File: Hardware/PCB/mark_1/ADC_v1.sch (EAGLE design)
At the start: 13 parts, among them IC1 MCP3424, IC2 MCP23017SO, Q1 IRLML6402, Q2 IRLML6402, Q3 IRLML6402, Q4 IRLML6402

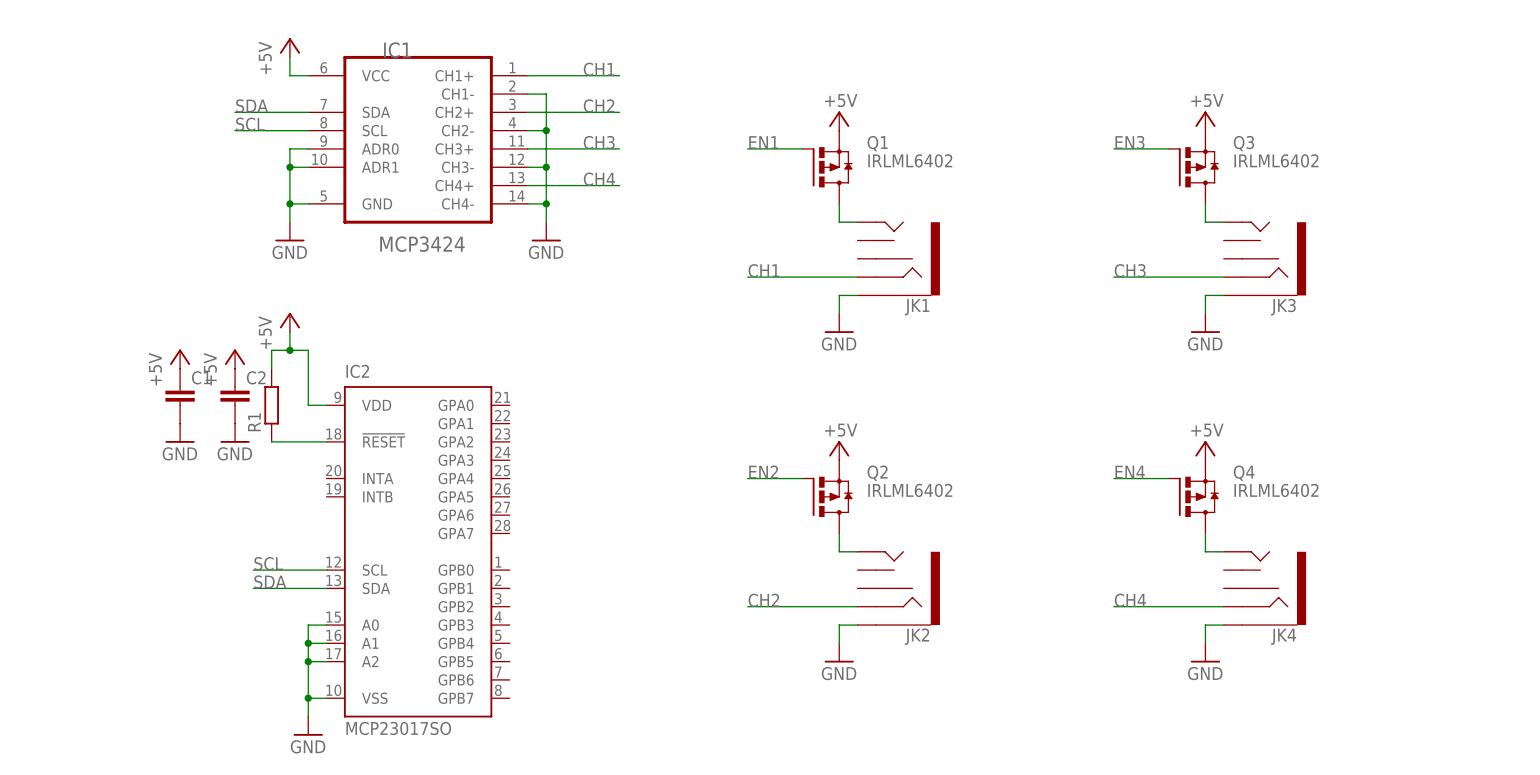
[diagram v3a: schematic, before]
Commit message: 
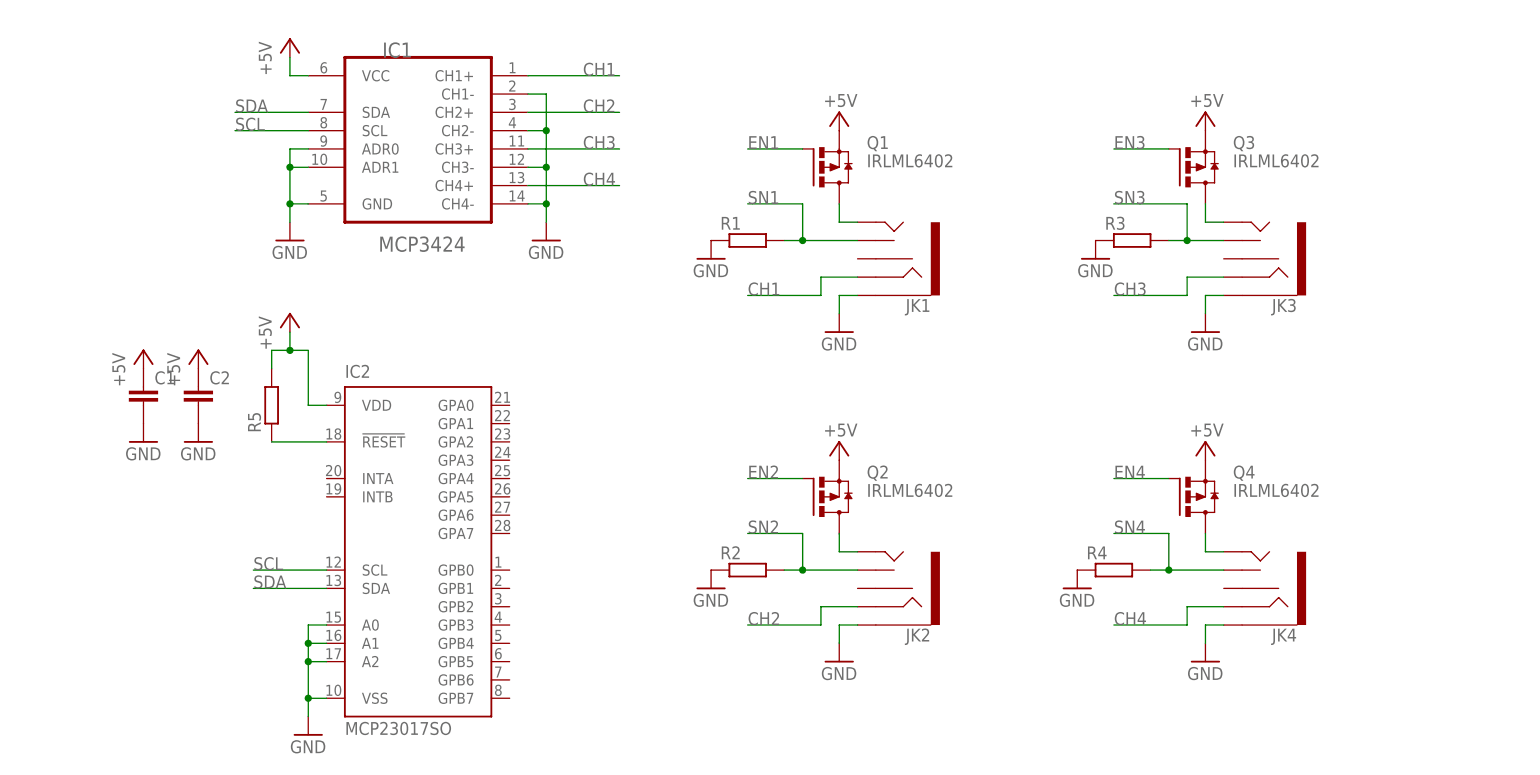
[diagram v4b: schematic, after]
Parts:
- added R2, R3, R4, R5: (no value), mark_1:R-EU_R0805
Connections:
- new net SN1: JK1.TSH, R1.2
- new net SN2: JK2.TSH, R2.2
- new net SN3: JK3.TSH, R3.2
- new net SN4: JK4.TSH, R4.2
- net +5V: now also R5.2; no longer R1.2
- net GND: now also R1.1, R2.1, R3.1, R4.1
- net N$2: now also R5.1; no longer R1.1
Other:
- moved on the sheet: C1, C2, R1
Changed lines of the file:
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@@
 <part name="IC2" library="mark_1" deviceset="MCP23017" device="SO"/>
 <part name="GND5" library="mark_1" deviceset="GND" device=""/>
-<part name="R1" library="mark_1" deviceset="R-EU_" device="R0805"/>
 <part name="P+4" library="mark_1" deviceset="+5V" device=""/>
 <part name="C2" library="mark_1" deviceset="C-EU" device="C0805K"/>
@@
 <part name="JK4" library="mark_1" deviceset="AUDIO-JACK2" device="PTH"/>
 <part name="GND9" library="mark_1" deviceset="GND" device=""/>
+<part name="R1" library="mark_1" deviceset="R-EU_" device="R0805"/>
+<part name="R2" library="mark_1" deviceset="R-EU_" device="R0805"/>
+<part name="R3" library="mark_1" deviceset="R-EU_" device="R0805"/>
+<part name="R4" library="mark_1" deviceset="R-EU_" device="R0805"/>
+<part name="GND10" library="mark_1" deviceset="GND" device=""/>
+<part name="GND11" library="mark_1" deviceset="GND" device=""/>
+<part name="GND12" library="mark_1" deviceset="GND" device=""/>
+<part name="GND13" library="mark_1" deviceset="GND" device=""/>
+<part name="R5" library="mark_1" deviceset="R-EU_" device="R0805"/>
 </parts>
 <sheets>
@@
 <instance part="P+2" gate="1" x="-124.46" y="93.98"/>
 <instance part="GND2" gate="1" x="-124.46" y="66.04"/>
-<instance part="C1" gate="G$1" x="-139.7" y="45.72"/>
-<instance part="P+3" gate="1" x="-139.7" y="50.8"/>
-<instance part="GND3" gate="1" x="-139.7" y="38.1"/>
+<instance part="C1" gate="G$1" x="-144.78" y="45.72"/>
+<instance part="P+3" gate="1" x="-144.78" y="50.8"/>
+<instance part="GND3" gate="1" x="-144.78" y="38.1"/>
 <instance part="IC2" gate="G$1" x="-106.68" y="22.86"/>
 <instance part="GND5" gate="1" x="-121.92" y="-2.54"/>
-<instance part="R1" gate="G$1" x="-127" y="43.18" rot="R90"/>
 <instance part="P+4" gate="1" x="-124.46" y="55.88"/>
-<instance part="C2" gate="G$1" x="-132.08" y="45.72"/>
-<instance part="P+5" gate="1" x="-132.08" y="50.8"/>
-<instance part="GND6" gate="1" x="-132.08" y="38.1"/>
+<instance part="C2" gate="G$1" x="-137.16" y="45.72"/>
+<instance part="P+5" gate="1" x="-137.16" y="50.8"/>
+<instance part="GND6" gate="1" x="-137.16" y="38.1"/>
 <instance part="JK1" gate="G$1" x="-40.64" y="63.5" rot="R180"/>
 <instance part="GND7" gate="1" x="-48.26" y="53.34"/>
@@
 <instance part="JK4" gate="G$1" x="10.16" y="17.78" rot="R180"/>
 <instance part="GND9" gate="1" x="2.54" y="7.62"/>
+<instance part="R1" gate="G$1" x="-60.96" y="66.04"/>
+<instance part="R2" gate="G$1" x="-60.96" y="20.32"/>
+<instance part="R3" gate="G$1" x="-7.62" y="66.04"/>
+<instance part="R4" gate="G$1" x="-10.16" y="20.32"/>
+<instance part="GND10" gate="1" x="-66.04" y="63.5"/>
+<instance part="GND11" gate="1" x="-12.7" y="63.5"/>
+<instance part="GND12" gate="1" x="-66.04" y="17.78"/>
+<instance part="GND13" gate="1" x="-15.24" y="17.78"/>
+<instance part="R5" gate="G$1" x="-127" y="43.18" rot="R90"/>
 </instances>
 <busses>
@@
 <wire x1="-121.92" y1="50.8" x2="-121.92" y2="43.18" width="0.1524" layer="91"/>
 <wire x1="-121.92" y1="43.18" x2="-119.38" y2="43.18" width="0.1524" layer="91"/>
-<pinref part="R1" gate="G$1" pin="2"/>
 <wire x1="-127" y1="48.26" x2="-127" y2="50.8" width="0.1524" layer="91"/>
 <wire x1="-127" y1="50.8" x2="-124.46" y2="50.8" width="0.1524" layer="91"/>
@@
 <wire x1="-124.46" y1="50.8" x2="-124.46" y2="53.34" width="0.1524" layer="91"/>
 <pinref part="P+4" gate="1" pin="+5V"/>
+<pinref part="R5" gate="G$1" pin="2"/>
 </segment>
 <segment>
@@
 <wire x1="2.54" y1="12.7" x2="5.08" y2="12.7" width="0.1524" layer="91"/>
 </segment>
+<segment>
+<pinref part="R1" gate="G$1" pin="1"/>
+<pinref part="GND10" gate="1" pin="GND"/>
+</segment>
+<segment>
+<pinref part="R3" gate="G$1" pin="1"/>
+<pinref part="GND11" gate="1" pin="GND"/>
+</segment>
+<segment>
+<pinref part="R2" gate="G$1" pin="1"/>
+<pinref part="GND12" gate="1" pin="GND"/>
+</segment>
+<segment>
+<pinref part="R4" gate="G$1" pin="1"/>
+<pinref part="GND13" gate="1" pin="GND"/>
+</segment>
 </net>
 <net name="CH1" class="0">
@@
 <segment>
 <pinref part="JK1" gate="G$1" pin="RING"/>
-<wire x1="-45.72" y1="60.96" x2="-60.96" y2="60.96" width="0.1524" layer="91"/>
-<label x="-60.96" y="60.96" size="1.778" layer="95"/>
+<wire x1="-45.72" y1="60.96" x2="-50.8" y2="60.96" width="0.1524" layer="91"/>
+<wire x1="-50.8" y1="60.96" x2="-50.8" y2="58.42" width="0.1524" layer="91"/>
+<wire x1="-50.8" y1="58.42" x2="-60.96" y2="58.42" width="0.1524" layer="91"/>
+<label x="-60.96" y="58.42" size="1.778" layer="95"/>
 </segment>
 </net>
@@
 <segment>
 <pinref part="JK2" gate="G$1" pin="RING"/>
-<wire x1="-45.72" y1="15.24" x2="-60.96" y2="15.24" width="0.1524" layer="91"/>
-<label x="-60.96" y="15.24" size="1.778" layer="95"/>
+<wire x1="-45.72" y1="15.24" x2="-50.8" y2="15.24" width="0.1524" layer="91"/>
+<wire x1="-50.8" y1="15.24" x2="-50.8" y2="12.7" width="0.1524" layer="91"/>
+<wire x1="-50.8" y1="12.7" x2="-60.96" y2="12.7" width="0.1524" layer="91"/>
+<label x="-60.96" y="12.7" size="1.778" layer="95"/>
 </segment>
 </net>
@@
 <segment>
 <pinref part="JK3" gate="G$1" pin="RING"/>
-<wire x1="5.08" y1="60.96" x2="-10.16" y2="60.96" width="0.1524" layer="91"/>
-<label x="-10.16" y="60.96" size="1.778" layer="95"/>
+<wire x1="5.08" y1="60.96" x2="0" y2="60.96" width="0.1524" layer="91"/>
+<wire x1="0" y1="60.96" x2="0" y2="58.42" width="0.1524" layer="91"/>
+<wire x1="0" y1="58.42" x2="-10.16" y2="58.42" width="0.1524" layer="91"/>
+<label x="-10.16" y="58.42" size="1.778" layer="95"/>
 </segment>
 </net>
@@
 <segment>
 <pinref part="JK4" gate="G$1" pin="RING"/>
-<wire x1="5.08" y1="15.24" x2="-10.16" y2="15.24" width="0.1524" layer="91"/>
-<label x="-10.16" y="15.24" size="1.778" layer="95"/>
+<wire x1="5.08" y1="15.24" x2="0" y2="15.24" width="0.1524" layer="91"/>
+<wire x1="0" y1="15.24" x2="0" y2="12.7" width="0.1524" layer="91"/>
+<wire x1="0" y1="12.7" x2="-10.16" y2="12.7" width="0.1524" layer="91"/>
+<label x="-10.16" y="12.7" size="1.778" layer="95"/>
 </segment>
 </net>
@@
 <net name="N$2" class="0">
 <segment>
-<pinref part="R1" gate="G$1" pin="1"/>
 <pinref part="IC2" gate="G$1" pin="!RESET"/>
 <wire x1="-127" y1="38.1" x2="-119.38" y2="38.1" width="0.1524" layer="91"/>
+<pinref part="R5" gate="G$1" pin="1"/>
 </segment>
 </net>
@@
 </segment>
 </net>
+<net name="SN1" class="0">
+<segment>
+<pinref part="JK1" gate="G$1" pin="TSH"/>
+<pinref part="R1" gate="G$1" pin="2"/>
+<wire x1="-55.88" y1="66.04" x2="-53.34" y2="66.04" width="0.1524" layer="91"/>
+<junction x="-53.34" y="66.04"/>
+<wire x1="-53.34" y1="66.04" x2="-45.72" y2="66.04" width="0.1524" layer="91"/>
+<wire x1="-53.34" y1="66.04" x2="-53.34" y2="71.12" width="0.1524" layer="91"/>
+<wire x1="-53.34" y1="71.12" x2="-60.96" y2="71.12" width="0.1524" layer="91"/>
+<label x="-60.96" y="71.12" size="1.778" layer="95"/>
+</segment>
+</net>
+<net name="SN2" class="0">
+<segment>
+<pinref part="JK2" gate="G$1" pin="TSH"/>
+<pinref part="R2" gate="G$1" pin="2"/>
+<wire x1="-55.88" y1="20.32" x2="-53.34" y2="20.32" width="0.1524" layer="91"/>
+<junction x="-53.34" y="20.32"/>
+<wire x1="-53.34" y1="20.32" x2="-45.72" y2="20.32" width="0.1524" layer="91"/>
+<wire x1="-53.34" y1="20.32" x2="-53.34" y2="25.4" width="0.1524" layer="91"/>
+<wire x1="-53.34" y1="25.4" x2="-60.96" y2="25.4" width="0.1524" layer="91"/>
+<label x="-60.96" y="25.4" size="1.778" layer="95"/>
+</segment>
+</net>
+<net name="SN3" class="0">
+<segment>
+<pinref part="JK3" gate="G$1" pin="TSH"/>
+<pinref part="R3" gate="G$1" pin="2"/>
+<wire x1="-2.54" y1="66.04" x2="0" y2="66.04" width="0.1524" layer="91"/>
+<junction x="0" y="66.04"/>
+<wire x1="0" y1="66.04" x2="5.08" y2="66.04" width="0.1524" layer="91"/>
+<wire x1="0" y1="66.04" x2="0" y2="71.12" width="0.1524" layer="91"/>
+<wire x1="0" y1="71.12" x2="-10.16" y2="71.12" width="0.1524" layer="91"/>
+<label x="-10.16" y="71.12" size="1.778" layer="95"/>
+</segment>
+</net>
+<net name="SN4" class="0">
+<segment>
+<pinref part="JK4" gate="G$1" pin="TSH"/>
+<pinref part="R4" gate="G$1" pin="2"/>
+<wire x1="-5.08" y1="20.32" x2="-2.54" y2="20.32" width="0.1524" layer="91"/>
+<junction x="-2.54" y="20.32"/>
+<wire x1="-2.54" y1="20.32" x2="5.08" y2="20.32" width="0.1524" layer="91"/>
+<wire x1="-2.54" y1="20.32" x2="-2.54" y2="25.4" width="0.1524" layer="91"/>
+<wire x1="-2.54" y1="25.4" x2="-10.16" y2="25.4" width="0.1524" layer="91"/>
+<label x="-10.16" y="25.4" size="1.778" layer="95"/>
+</segment>
+</net>
